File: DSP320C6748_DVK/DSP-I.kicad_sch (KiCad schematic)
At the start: 1 part, among them U1 TMS320C6748EZWT4

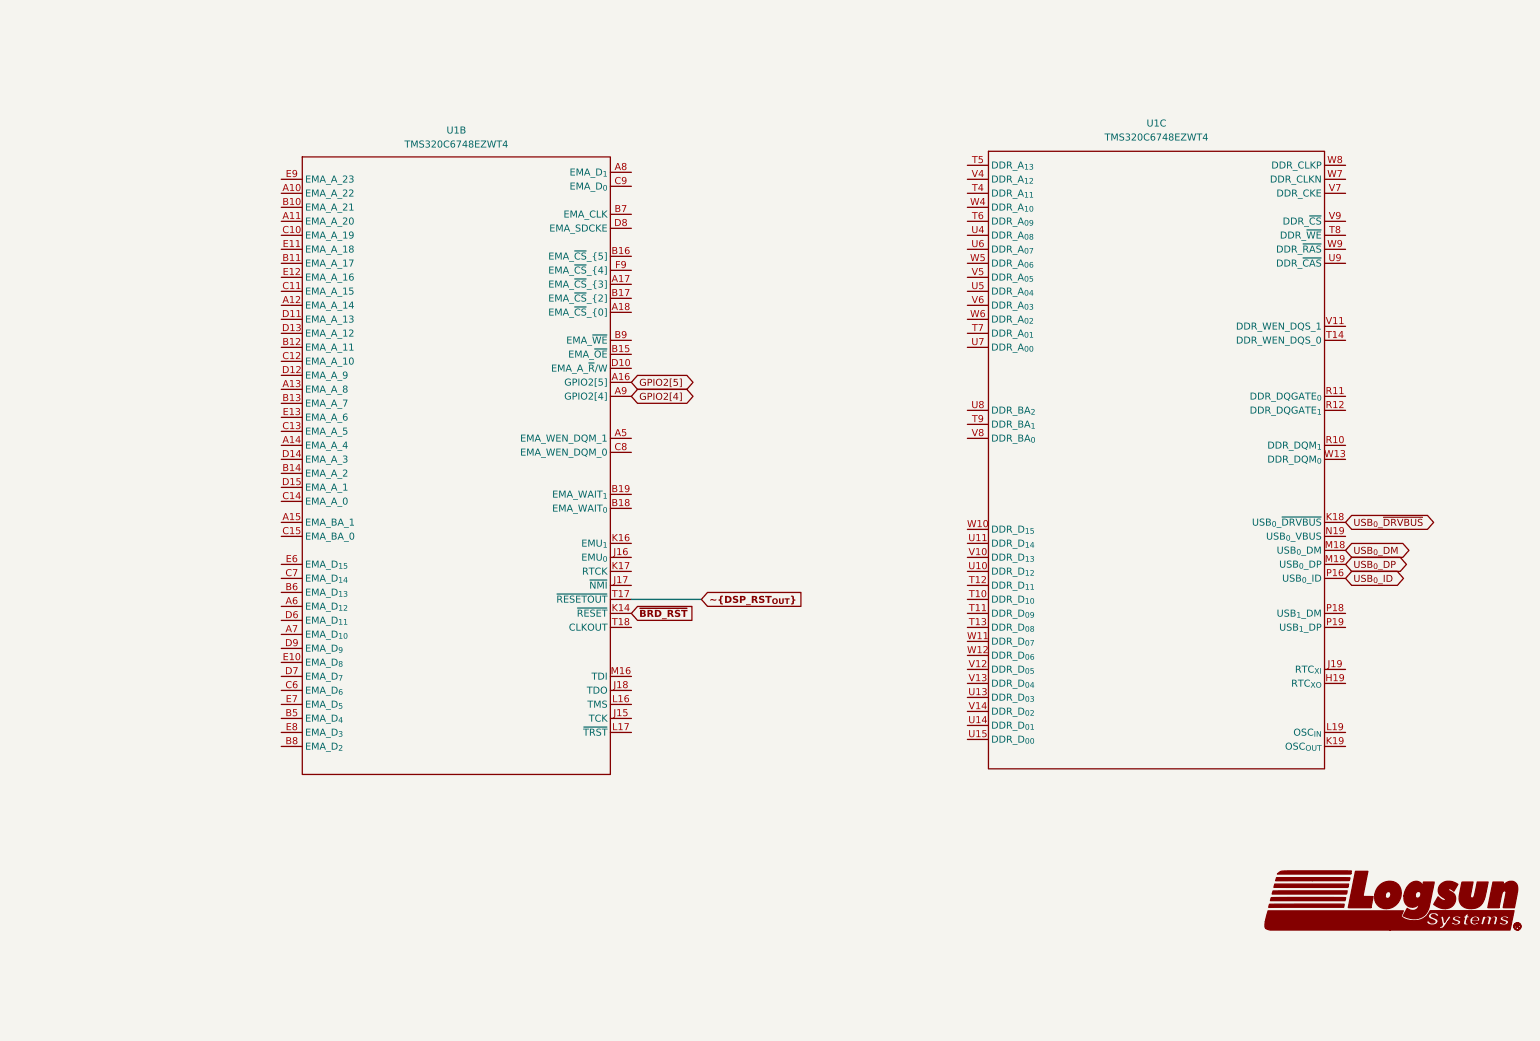
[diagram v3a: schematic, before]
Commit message: Partial VGA-LCD schematic added
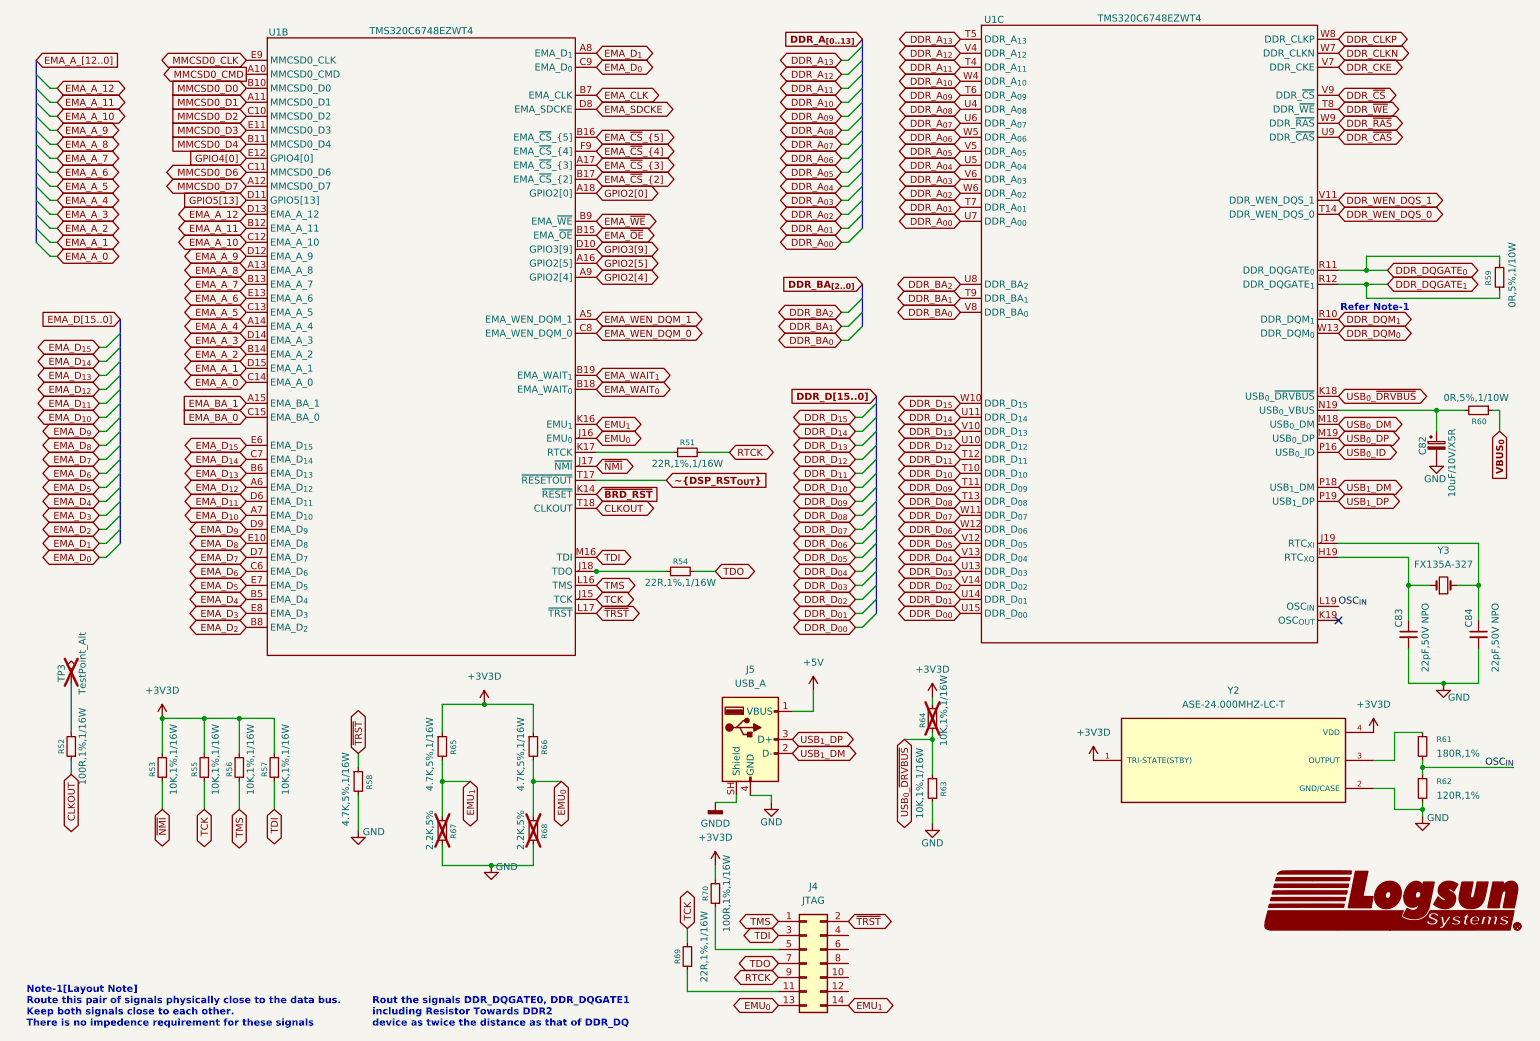
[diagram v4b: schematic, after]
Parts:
- added C82: 10uF/10V/X5R, symbol Device:C_Polarized_Small
- added C83, C84: 22pF,50V NPO, symbol Device:C_Small
- added J4: JTAG, symbol Connector_Generic:Conn_02x07_Odd_Even
- added J5: USB_A, symbol Connector:USB_A
- added R51, R54, R69: 22R,1%,1/16W, symbol Device:R_Small
- added R52, R70: 100R,1%,1/16W, symbol Device:R_Small
- added R53, R55, R56, R57, R63, R64: 10K,1%,1/16W, symbol Device:R_Small
- added R58, R65, R66: 4.7K,5%,1/16W, symbol Device:R_Small
- added R59, R60: 0R,5%,1/10W, symbol Device:R_Small
- added R61: 180R,1%, symbol Device:R_Small
- added R62: 120R,1%, symbol Device:R_Small
- added R67, R68: 2.2K,5%, symbol Device:R_Small
- added TP3: TestPoint_Alt, symbol Connector:TestPoint_Alt
- added Y2: ASE-24.000MHZ-LC-T, ASE-24.000MHZ-LC-T:XTAL_ASE-24.000MHZ-LC-T, symbol ASE-24.000MHZ-LC-T:ASE-24.000MHZ-LC-T
- added Y3: FX135A-327, symbol Device:Crystal_Small
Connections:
- net USB_{0}_~{DRVBUS}: now also R63.2, R64.1
- net MMCSD0_CMD: now reaches U1.A10 (EMA_A_22)
- net MMCSD0_D1: now reaches U1.A11 (EMA_A_20)
- net MMCSD0_D7: now reaches U1.A12 (EMA_A_14)
- net EMA_A_8: now reaches U1.A13 (EMA_A_8)
- net EMA_A_4: now reaches U1.A14 (EMA_A_4)
- net EMA_BA_1: now reaches U1.A15 (EMA_BA_1)
- net EMA_~{CS}_{3]: now reaches U1.A17 (EMA_~{CS}_{3])
- net GPIO2[0]: now reaches U1.A18 (EMA_~{CS}_{0])
- net EMA_WEN_DQM_1: now reaches U1.A5 (EMA_WEN_DQM_1)
- net EMA_D_{12}: now reaches U1.A6 (EMA_D_{12})
- net EMA_D_{10}: now reaches U1.A7 (EMA_D_{10})
- net EMA_D_{1}: now reaches U1.A8 (EMA_D_{1})
- net MMCSD0_D0: now reaches U1.B10 (EMA_A_21)
- net MMCSD0_D4: now reaches U1.B11 (EMA_A_17)
- net EMA_A_11: now reaches U1.B12 (EMA_A_11)
- net EMA_A_7: now reaches U1.B13 (EMA_A_7)
- net EMA_A_2: now reaches U1.B14 (EMA_A_2)
- net EMA_~{OE}: now reaches U1.B15 (EMA_~{OE})
- net EMA_~{CS}_{5]: now reaches U1.B16 (EMA_~{CS}_{5])
- net EMA_~{CS}_{2]: now reaches U1.B17 (EMA_~{CS}_{2])
- net EMA_WAIT_{0}: now reaches U1.B18 (EMA_WAIT_{0})
- net EMA_WAIT_{1}: now reaches U1.B19 (EMA_WAIT_{1})
- net EMA_D_{4}: now reaches U1.B5 (EMA_D_{4})
- net EMA_D_{13}: now reaches U1.B6 (EMA_D_{13})
- net EMA_CLK: now reaches U1.B7 (EMA_CLK)
- net EMA_D_{2}: now reaches U1.B8 (EMA_D_{2})
- net EMA_~{WE}: now reaches U1.B9 (EMA_~{WE})
- net MMCSD0_D2: now reaches U1.C10 (EMA_A_19)
- net MMCSD0_D6: now reaches U1.C11 (EMA_A_15)
- net EMA_A_10: now reaches U1.C12 (EMA_A_10)
- net EMA_A_5: now reaches U1.C13 (EMA_A_5)
- net EMA_A_0: now reaches U1.C14 (EMA_A_0)
- net EMA_BA_0: now reaches U1.C15 (EMA_BA_0)
- net EMA_D_{6}: now reaches U1.C6 (EMA_D_{6})
- net EMA_D_{14}: now reaches U1.C7 (EMA_D_{14})
- net EMA_WEN_DQM_0: now reaches U1.C8 (EMA_WEN_DQM_0)
- net EMA_D_{0}: now reaches U1.C9 (EMA_D_{0})
- net GPIO3[9]: now reaches U1.D10 (EMA_A_~{R}/W)
- net GPIO5[13]: now reaches U1.D11 (EMA_A_13)
- net EMA_A_9: now reaches U1.D12 (EMA_A_9)
- net EMA_A_12: now reaches U1.D13 (EMA_A_12)
- net EMA_A_3: now reaches U1.D14 (EMA_A_3)
- net EMA_A_1: now reaches U1.D15 (EMA_A_1)
- net EMA_D_{11}: now reaches U1.D6 (EMA_D_{11})
- net EMA_D_{7}: now reaches U1.D7 (EMA_D_{7})
- net EMA_SDCKE: now reaches U1.D8 (EMA_SDCKE)
- net EMA_D_{9}: now reaches U1.D9 (EMA_D_{9})
- net EMA_D_{8}: now reaches U1.E10 (EMA_D_{8})
- net MMCSD0_D3: now reaches U1.E11 (EMA_A_18)
- net GPIO4[0]: now reaches U1.E12 (EMA_A_16)
- net EMA_A_6: now reaches U1.E13 (EMA_A_6)
- net EMA_D_{15}: now reaches U1.E6 (EMA_D_{15})
- net EMA_D_{5}: now reaches U1.E7 (EMA_D_{5})
- net EMA_D_{3}: now reaches U1.E8 (EMA_D_{3})
- net MMCSD0_CLK: now reaches U1.E9 (EMA_A_23)
- net EMA_~{CS}_{4]: now reaches U1.F9 (EMA_~{CS}_{4])
- net TCK: now reaches U1.J15 (TCK)
- net TCK: now also R55.1, R69.2
- net EMU_{0}: now reaches U1.J16 (EMU_{0})
- net EMU_{0}: now also J4.13 (Pin_13), R66.2, R68.1
- net ~{NMI}: now reaches U1.J17 (~{NMI})
- net ~{NMI}: now also R53.1
- net at U1.J18 (TDO): now also R54.1
- net EMU_{1}: now reaches U1.K16 (EMU_{1})
- net EMU_{1}: now also J4.14 (Pin_14), R65.2, R67.1
- net at U1.K17 (RTCK): now also R51.1
- net TMS: now reaches U1.L16 (TMS)
- net TMS: now also J4.1 (Pin_1), R56.1
- net ~{TRST}: now reaches U1.L17 (~{TRST})
- net ~{TRST}: now also J4.2 (Pin_2), R58.1
- net TDI: now reaches U1.M16 (TDI)
- net TDI: now also J4.3 (Pin_3), R57.1
- net CLKOUT: now reaches U1.T18 (CLKOUT)
- net CLKOUT: now also R52.1
- net at U1.H19 (RTC_{XO}): now also C83.1, Y3.1
- net at U1.J19 (RTC_{XI}): now also C84.1, Y3.2
- net OSC_{IN}: now reaches U1.L19 (OSC_{IN})
- net OSC_{IN}: now also R61.2, R62.1
- net at U1.N19 (USB_{0}_VBUS): now also C82.1, R60.2
- net USB_{1}_DM: now reaches U1.P18 (USB_{1}_DM)
- net USB_{1}_DM: now also J5.2 (D-)
- net USB_{1}_DP: now reaches U1.P19 (USB_{1}_DP)
- net USB_{1}_DP: now also J5.3 (D+)
- net DDR_DQM_{1}: now reaches U1.R10 (DDR_DQM_{1})
- net DDR_DQGATE_{0}: now reaches U1.R11 (DDR_DQGATE_{0})
- net DDR_DQGATE_{0}: now also R59.2
- net DDR_DQGATE_{1}: now reaches U1.R12 (DDR_DQGATE_{1})
- net DDR_DQGATE_{1}: now also R59.1
- net DDR_D_{10}: now reaches U1.T10 (DDR_D_{10})
- net DDR_D_{09}: now reaches U1.T11 (DDR_D_{09})
- net DDR_D_{11}: now reaches U1.T12 (DDR_D_{11})
- net DDR_D_{08}: now reaches U1.T13 (DDR_D_{08})
- net DDR_WEN_DQS_0: now reaches U1.T14 (DDR_WEN_DQS_0)
- net DDR_A_{11}: now reaches U1.T4 (DDR_A_{11})
- net DDR_A_{13}: now reaches U1.T5 (DDR_A_{13})
- net DDR_A_{09}: now reaches U1.T6 (DDR_A_{09})
- net DDR_A_{01}: now reaches U1.T7 (DDR_A_{01})
- net DDR_~{WE}: now reaches U1.T8 (DDR_~{WE})
- net DDR_BA_{1}: now reaches U1.T9 (DDR_BA_{1})
- net DDR_D_{12}: now reaches U1.U10 (DDR_D_{12})
- net DDR_D_{14}: now reaches U1.U11 (DDR_D_{14})
- net DDR_D_{03}: now reaches U1.U13 (DDR_D_{03})
- net DDR_D_{01}: now reaches U1.U14 (DDR_D_{01})
- net DDR_D_{00}: now reaches U1.U15 (DDR_D_{00})
- net DDR_A_{08}: now reaches U1.U4 (DDR_A_{08})
- net DDR_A_{04}: now reaches U1.U5 (DDR_A_{04})
- net DDR_A_{07}: now reaches U1.U6 (DDR_A_{07})
- net DDR_A_{00}: now reaches U1.U7 (DDR_A_{00})
- net DDR_BA_{2}: now reaches U1.U8 (DDR_BA_{2})
- net DDR_~{CAS}: now reaches U1.U9 (DDR_~{CAS})
- net DDR_D_{13}: now reaches U1.V10 (DDR_D_{13})
- net DDR_WEN_DQS_1: now reaches U1.V11 (DDR_WEN_DQS_1)
- net DDR_D_{05}: now reaches U1.V12 (DDR_D_{05})
- net DDR_D_{04}: now reaches U1.V13 (DDR_D_{04})
- net DDR_D_{02}: now reaches U1.V14 (DDR_D_{02})
- net DDR_A_{12}: now reaches U1.V4 (DDR_A_{12})
- net DDR_A_{05}: now reaches U1.V5 (DDR_A_{05})
- net DDR_A_{03}: now reaches U1.V6 (DDR_A_{03})
- net DDR_CKE: now reaches U1.V7 (DDR_CKE)
- net DDR_BA_{0}: now reaches U1.V8 (DDR_BA_{0})
- net DDR_~{CS}: now reaches U1.V9 (DDR_~{CS})
- net DDR_D_{15}: now reaches U1.W10 (DDR_D_{15})
- net DDR_D_{07}: now reaches U1.W11 (DDR_D_{07})
- net DDR_D_{06}: now reaches U1.W12 (DDR_D_{06})
- net DDR_DQM_{0}: now reaches U1.W13 (DDR_DQM_{0})
- net DDR_A_{10}: now reaches U1.W4 (DDR_A_{10})
- net DDR_A_{06}: now reaches U1.W5 (DDR_A_{06})
- net DDR_A_{02}: now reaches U1.W6 (DDR_A_{02})
- net DDR_CLKN: now reaches U1.W7 (DDR_CLKN)
- net DDR_CLKP: now reaches U1.W8 (DDR_CLKP)
- net DDR_~{RAS}: now reaches U1.W9 (DDR_~{RAS})
- new net: R52.2, TP3.1
- new net: J4.5 (Pin_5), R70.1
- new net: R61.1, Y2.3 (OUTPUT)
- new net: J4.11 (Pin_11), R69.1
- new net +3V3D: R53.2, R55.2, R56.2, R57.2, R64.2, R65.1, R66.1, R70.2, Y2.1 (TRI-STATE(STBY)), Y2.4 (VDD)
- new net +5V: J5.1 (VBUS)
- new net GND: C82.2, C83.2, C84.2, J5.4 (GND), R58.2, R62.2, R63.1, R67.2, R68.2, Y2.2 (GND/CASE)
- new net GNDD: J5.SH (Shield)
- new net RTCK: J4.9 (Pin_9), R51.2
- new net TDO: J4.7 (Pin_7), R54.2
- new net VBUS_{0}: R60.1
- no-connect marks 0 -> 1
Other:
- note added: "Note-1[Layout Note] Route this pair of signals physically close to the data bus. Keep both signals close to each other. There is no impedence requirement for these signals"
- note added: "Refer Note-1"
- note added: "Rout the signals DDR_DQGATE0, DDR_DQGATE1 including Resistor Towards DDR2 device as twice the distance as that of DDR_DQ"
- moved on the sheet: U1B, U1C

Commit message: DDR_RAM and Video Decoder Schematic Added
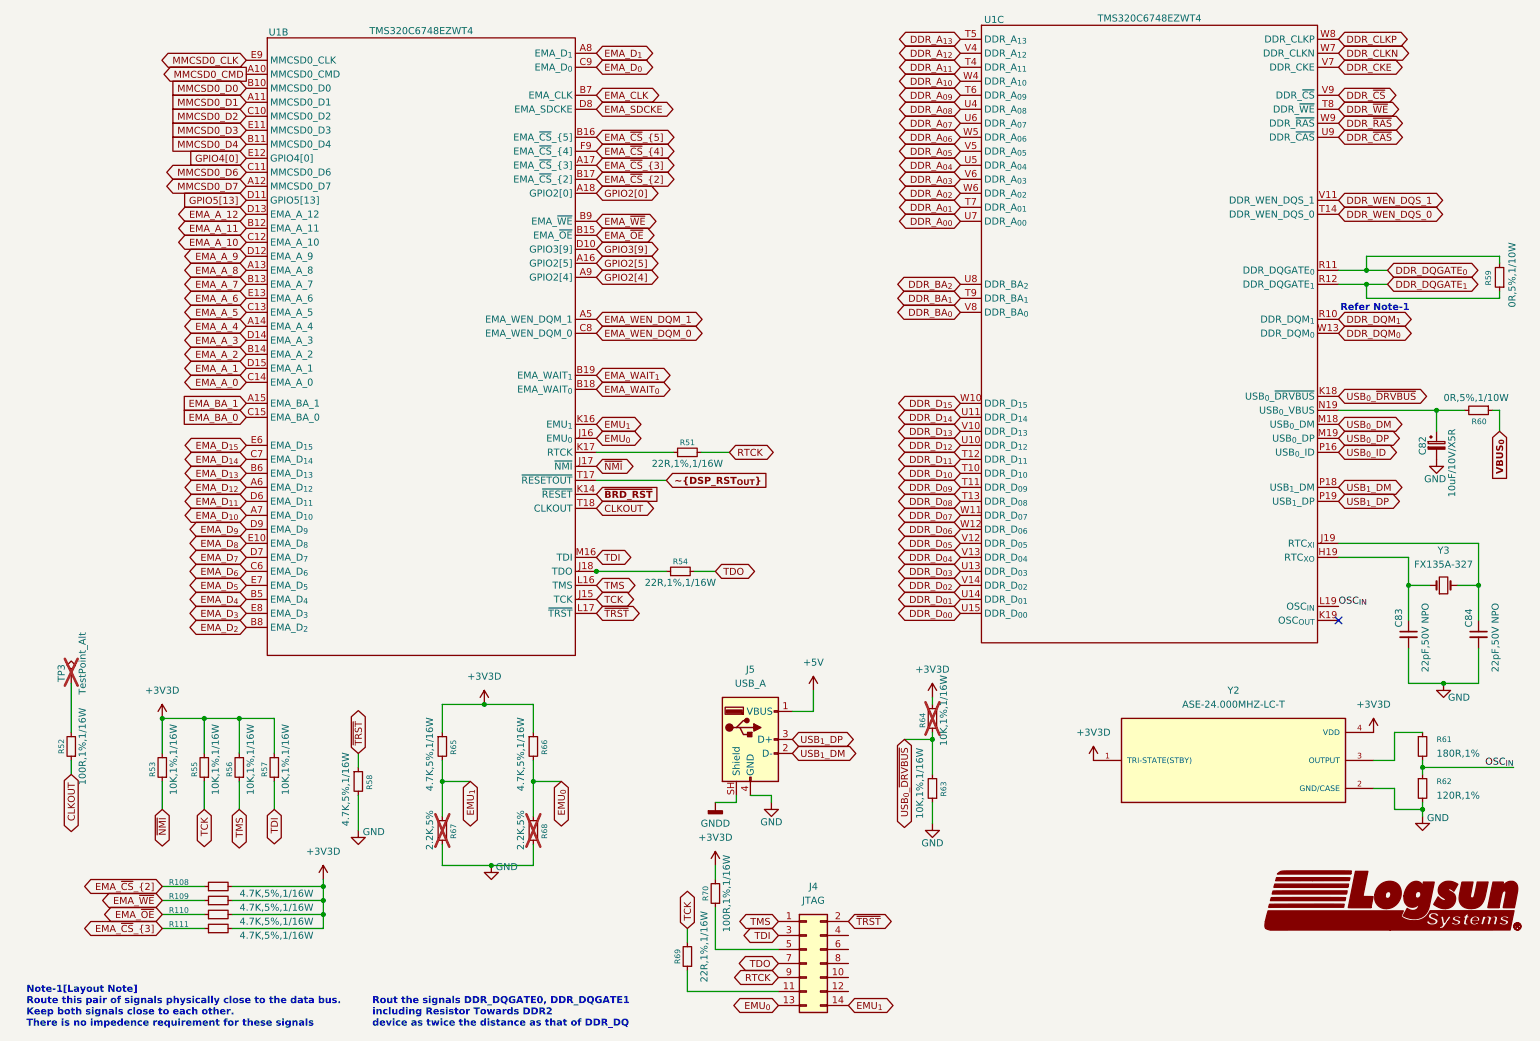
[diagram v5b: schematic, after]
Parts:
- added R108, R109, R110, R111: 4.7K,5%,1/16W, symbol Device:R_Small
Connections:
- net +3V3D: now also R108.2, R109.2, R110.2, R111.2
- net EMA_~{CS}_{2]: now also R108.1
- net EMA_~{CS}_{3]: now also R111.1
- net EMA_~{OE}: now also R110.1
- net EMA_~{WE}: now also R109.1

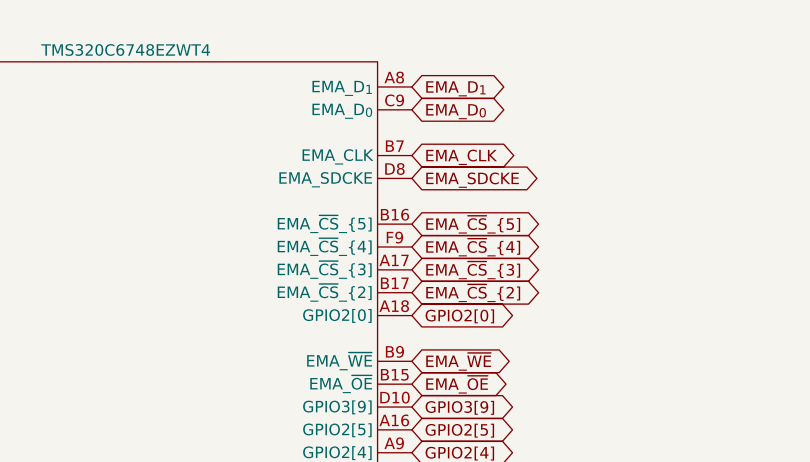
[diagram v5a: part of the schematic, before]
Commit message: Connectors and mislleneous components added
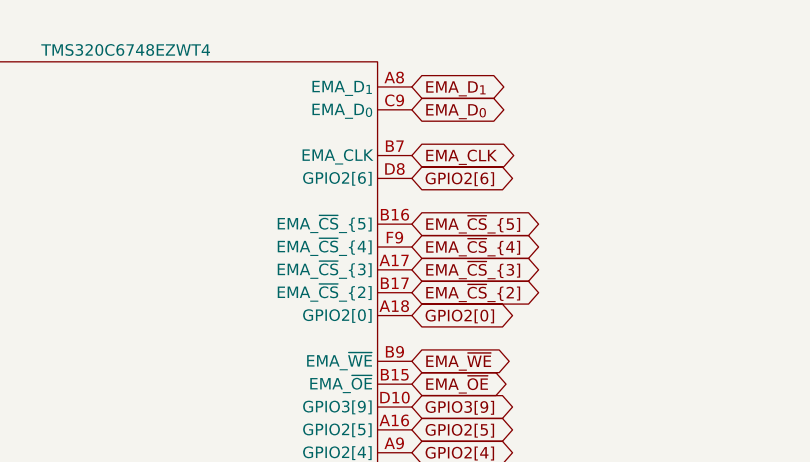
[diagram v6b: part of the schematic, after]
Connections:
- net EMA_SDCKE renamed GPIO2[6]
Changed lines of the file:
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@@
 		)
 	)
+	(global_label "GPIO2[6]"
+		(shape bidirectional)
+		(at 115.57 30.48 0)
+		(effects
+			(font
+				(size 1.27 1.27)
+			)
+			(justify left)
+		)
+		(property "Intersheetrefs" "${INTERSHEET_REFS}"
+			(at 115.57 30.48 0)
+			(hide yes)
+			(show_name no)
+			(do_not_autoplace no)
+			(effects
+				(font
+					(size 1.27 1.27)
+				)
+			)
+		)
+	)
 	(global_label "DDR_A_{12}"
 		(shape bidirectional)
@@
 		)
 	)
-	(global_label "EMA_SDCKE"
-		(shape bidirectional)
-		(at 115.57 30.48 0)
-		(effects
-			(font
-				(size 1.27 1.27)
-			)
-			(justify left)
-		)
-		(property "Intersheetrefs" "${INTERSHEET_REFS}"
-			(at 115.57 30.48 0)
-			(hide yes)
-			(show_name no)
-			(do_not_autoplace no)
-			(effects
-				(font
-					(size 1.27 1.27)
-				)
-			)
-		)
-	)
 	(global_label "EMA_A_10"
 		(shape bidirectional)
@@
 		)
 		(pin "D8"
+			(alternate "GPIO2[6]")
 		)
 		(pin "B16"

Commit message: Whole Schematic Reannotation Done
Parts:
- renumbered C83 to C47, C82 to C48, C84 to C49, J5 to J1, J4 to J2, R111 to R10, R56 to R11, R57 to R12, R58 to R13, R65 to R14, R67 to R15, R66 to R16, R68 to R17, R54 to R18, R51 to R19, R69 to R20, R70 to R21, R64 to R22, R63 to R23, R61 to R24, R62 to R25, R60 to R26, R59 to R27, R52 to R4, R53 to R5, R55 to R6, R108 to R7, R109 to R8, R110 to R9, TP3 to TP1, Y2 to Y1, Y3 to Y2

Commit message: Schematic corrections-I
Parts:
- added C204: 0.1uF/16V/X7R, symbol Device:C_Small
- added FB15: MMZ2012S121A, symbol Device:FerriteBead_Small
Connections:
- net +3V3D: now also C204.1
- net GND: now also C204.2, FB15.2; no longer C47.2, C49.2
- net GNDD: now also FB15.1
- new net RTC_VSS: C47.2, C49.2
